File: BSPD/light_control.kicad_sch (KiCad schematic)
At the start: 1 part, among them U25 MAX351ESE-T

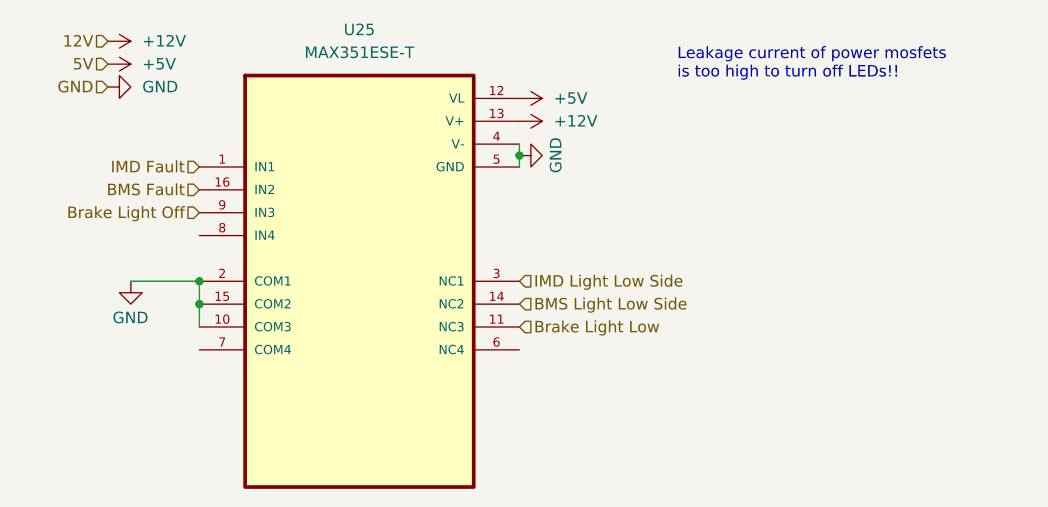
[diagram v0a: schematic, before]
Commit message: Overhaul of BPSD to V3.0
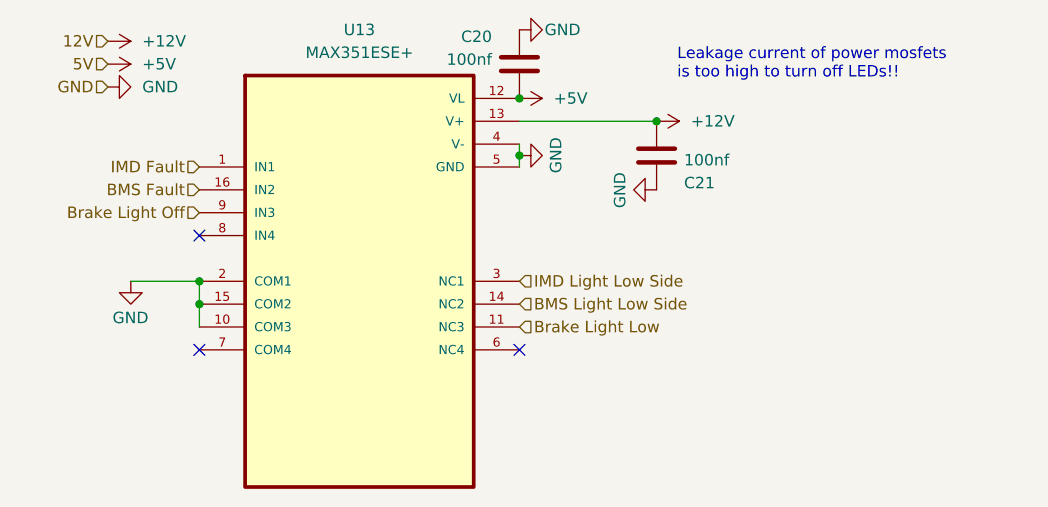
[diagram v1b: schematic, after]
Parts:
- added C20, C21: 100nf, Capacitor_SMD:C_0805_2012Metric_Pad1.18x1.45mm_HandSolder, symbol Device:C
- U13: renamed from U25; value MAX351ESE-T -> MAX351ESE+
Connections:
- net +12V: now also C21.1
- net +5V: now also C20.1
- net GND: now also C20.2, C21.2
- no-connect marks 0 -> 3
